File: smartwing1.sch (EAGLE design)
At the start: 27 parts, among them IC3 PIC24FJ64GB002, SW1 CT10-XXXX-A2, U1 MPL115A2, U2 MPU-6050, U3 SAM-M8Q

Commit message: Ajout_composant_axelle
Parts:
- added U$1: 992_MPL115A2, 2S_AW_lib:992_MPL115A2
- added U$2: MIKROE-2045, 2S_AW_lib:MIKROE-2045
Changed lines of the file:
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@@
 <part name="P+10" library="supply1" library_urn="urn:adsk.eagle:library:371" deviceset="VCC" device=""/>
 <part name="X_14" library="ngspice-simulation" library_urn="urn:adsk.eagle:library:527439" deviceset="GND" device=""/>
+<part name="U$1" library="2S_AW_lib" deviceset="992_MPL115A2" device=""/>
+<part name="U$2" library="2S_AW_lib" deviceset="MIKROE-2045" device=""/>
 </parts>
 <sheets>
@@
 </instance>
 <instance part="X_14" gate="G$1" x="708.66" y="15.24" smashed="yes" rot="R270"/>
+<instance part="U$1" gate="G$1" x="825.5" y="-116.84" smashed="yes">
+<attribute name="NAME" x="820.42" y="-111.76" size="1.778" layer="95"/>
+<attribute name="VALUE" x="820.42" y="-116.84" size="1.778" layer="96"/>
+</instance>
+<instance part="U$2" gate="G$1" x="894.08" y="-129.54" smashed="yes">
+<attribute name="NAME" x="889" y="-121.92" size="1.778" layer="95"/>
+<attribute name="VALUE" x="889" y="-127" size="1.778" layer="96"/>
+</instance>
 </instances>
 <busses>

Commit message: Branchements_comp_ax
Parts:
- added C12, C5: 0.1uF, rcl:C-EU075-032X103
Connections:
- removed net N$13: IC3.AN4/C1INB/DPLN/SDA2/RP2/PMD2/CN6/RB2
- removed net N$16: IC3.AN5/C1INA/DMLN/RTCC/SCL2/RP3/PMWR/CN7/RB3
- removed net N$24: IC3.TCK/USBOEN/SCL1/RP8/PMD4/CN22/RB8
- removed net N$25: IC3.TDO/SDA1/RP9/PMD3/RCV/CN21/RB9
- new net GPS_RX: U$2.RX
- new net GPS_TX: U$2.TX
- new net MPL_SCL: IC3.TCK/USBOEN/SCL1/RP8/PMD4/CN22/RB8, U$1.SCL
- new net MPL_SDA: IC3.TDO/SDA1/RP9/PMD3/RCV/CN21/RB9, U$1.SDA
- net 0: now also U$2.GND2
- net GND: now also C12.2, C5.2, U$1.GND, U$2.GND
- net VCC: now also C12.1, C5.1, U$1.VDD, U$2.3.3V
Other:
- note added: "14/06/2020"
- note added: "2S8"
- moved on the sheet: U$1, U$2

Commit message: on komance ah avouare un vurai truk
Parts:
- removed U1: MPL115A2, untitled:MPL115A2
- removed U3: SAM-M8Q, SAM_M8Q:SAM-M8Q
- added C13: 0.1uF, rcl:C-EU075-032X103
- added R4, R5, R6, R7: 4.7k, rcl:R-EU_0207/7
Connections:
- new net MPU_SCL: IC3.TCK/USBOEN/SCL1/RP8/PMD4/CN22/RB8, R6.2, U2.SCL
- new net MPU_SDA: IC3.TDO/SDA1/RP9/PMD3/RCV/CN21/RB9, R7.1, U2.SDA
- new net N$1: U$1.RST
- new net N$10: U2.NC_4
- new net N$11: U2.NC_5
- new net N$14: U2.VLOGIC
- new net N$15: U2.AD0
- new net N$16: U2.REGOUT
- new net N$19: U2.FSYNC
- new net N$20: U2.INT
- new net N$21: C13.1, U2.VDD
- new net N$24: U2.NC_6
- new net N$25: U2.NC_7
- new net N$27: U2.NC_8
- new net N$29: U2.NC
- new net N$31: U2.RESV_2
- new net N$32: U2.CPOUT
- new net N$33: U2.RESV_3
- new net N$34: U2.RESV
- new net N$37: U2.25
- new net N$9: U2.NC_3
- net GND: now also U2.GND
- net GPS_RX: now also IC3.PGEC3/AN1/C3IND/VREF-/ASCL1(2)/RP6/RA1
- net GPS_TX: now also IC3.PGED3/AN0/C3INC/VREF+/ASDA1(2)/RP5/RA0
- net MPL_SCL: now also R5.2, U2.AUX_CL; no longer IC3.TCK/USBOEN/SCL1/RP8/PMD4/CN22/RB8
- net MPL_SDA: now also R4.2, U2.AUX_DA; no longer IC3.TDO/SDA1/RP9/PMD3/RCV/CN21/RB9
- net N$3: now also U2.CLKIN; no longer IC3.PGED3/AN0/C3INC/VREF+/ASDA1(2)/RP5/RA0
- net N$4: now also U2.NC_2; no longer IC3.PGEC3/AN1/C3IND/VREF-/ASCL1(2)/RP6/RA1
- net VCC: now also C13.2, R4.1, R5.1, R6.1, R7.2

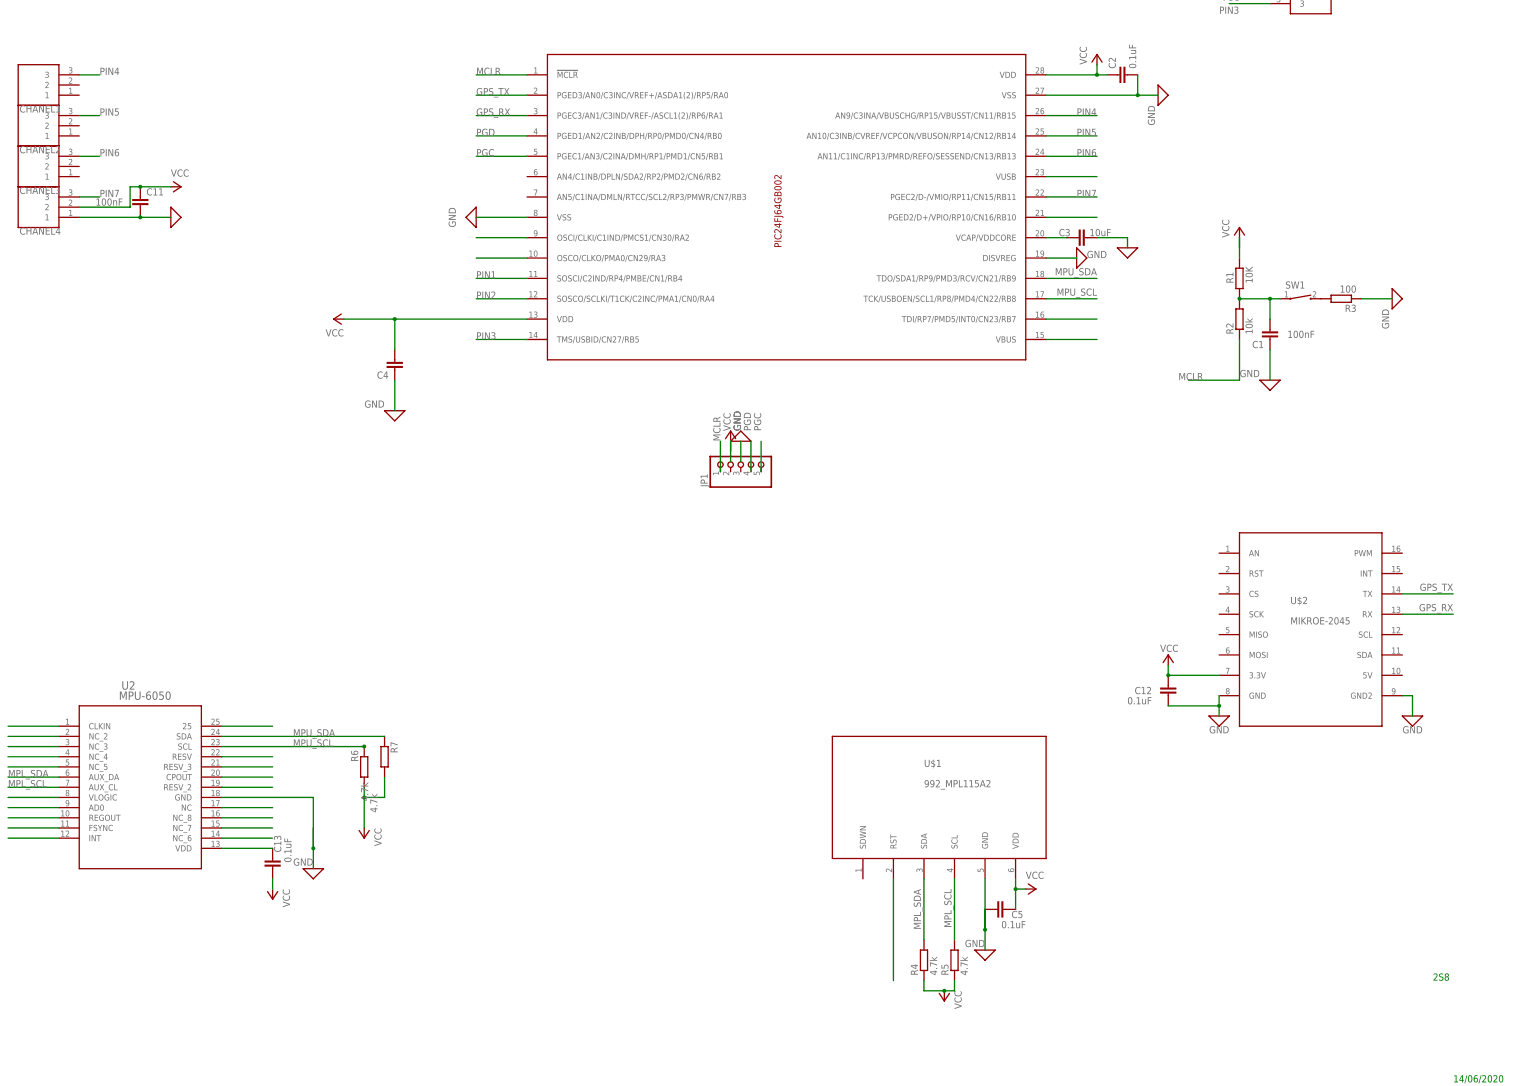
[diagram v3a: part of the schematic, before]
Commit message: Add SEN0142/UART
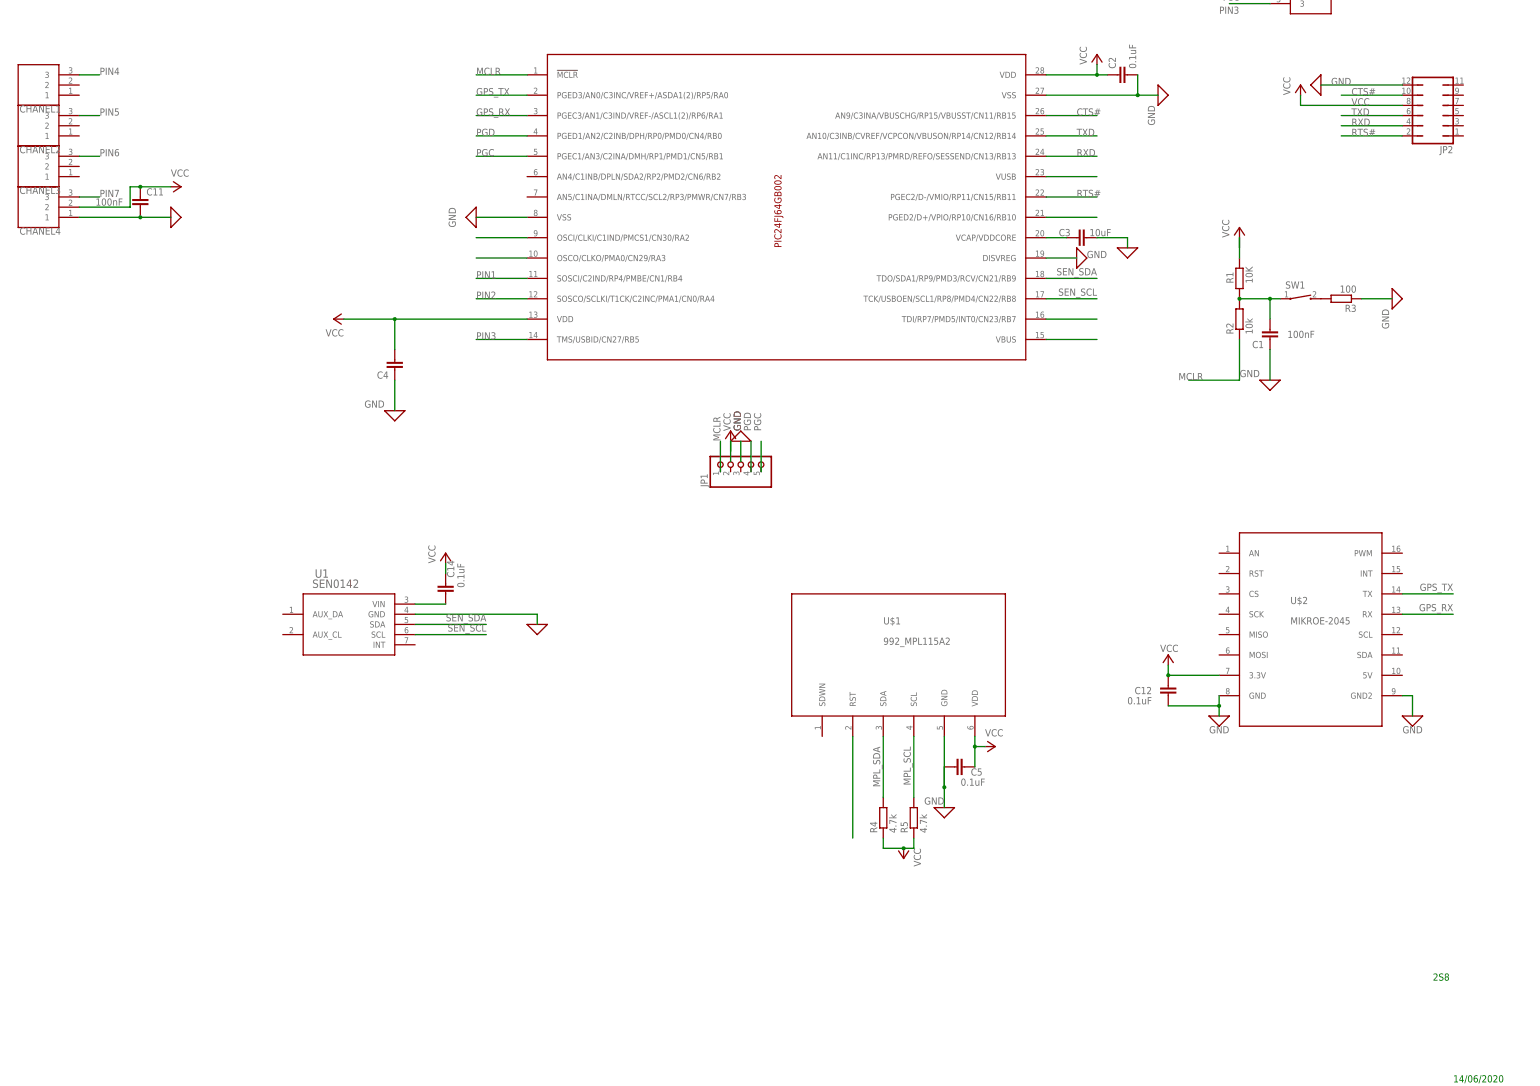
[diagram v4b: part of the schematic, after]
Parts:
- removed C13: 0.1uF, rcl:C-EU075-032X103
- removed R6, R7: 4.7k, rcl:R-EU_0207/7
- removed U2: MPU-6050, MPU6050:MPU-6050
- added C14: 0.1uF, rcl:C-EU075-032X103
- added JP2: (no value), jumper:JP6Q
- added U1: SEN0142, MPU6050:SEN0142
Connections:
- removed net MPU_SCL: IC3.TCK/USBOEN/SCL1/RP8/PMD4/CN22/RB8, R6.2, U2.SCL
- removed net MPU_SDA: IC3.TDO/SDA1/RP9/PMD3/RCV/CN21/RB9, R7.1, U2.SDA
- removed net N$10: U2.NC_4
- removed net N$11: U2.NC_5
- removed net N$14: U2.VLOGIC
- removed net N$15: U2.AD0
- removed net N$16: U2.REGOUT
- removed net N$19: U2.FSYNC
- removed net N$20: U2.INT
- removed net N$21: C13.1, U2.VDD
- removed net N$24: U2.NC_6
- removed net N$25: U2.NC_7
- removed net N$27: U2.NC_8
- removed net N$29: U2.NC
- removed net N$3: U2.CLKIN
- removed net N$31: U2.RESV_2
- removed net N$32: U2.CPOUT
- removed net N$33: U2.RESV_3
- removed net N$34: U2.RESV
- removed net N$37: U2.25
- removed net N$4: U2.NC_2
- removed net N$9: U2.NC_3
- new net CTS#: IC3.AN9/C3INA/VBUSCHG/RP15/VBUSST/CN11/RB15, JP2.10
- new net N$12: C14.2, U1.VIN
- new net RTS#: IC3.PGEC2/D-/VMIO/RP11/CN15/RB11, JP2.2
- new net RXD: IC3.AN11/C1INC/RP13/PMRD/REFO/SESSEND/CN13/RB13, JP2.4
- new net SEN_SCL: IC3.TCK/USBOEN/SCL1/RP8/PMD4/CN22/RB8, U1.SCL
- new net SEN_SDA: IC3.TDO/SDA1/RP9/PMD3/RCV/CN21/RB9, U1.SDA
- new net TXD: IC3.AN10/C3INB/CVREF/VCPCON/VBUSON/RP14/CN12/RB14, JP2.6
- net 0: now also U1.GND
- net GND: now also JP2.12; no longer U2.GND
- net MPL_SCL: no longer U2.AUX_CL
- net MPL_SDA: no longer U2.AUX_DA
- net PIN4: no longer IC3.AN9/C3INA/VBUSCHG/RP15/VBUSST/CN11/RB15
- net PIN5: no longer IC3.AN10/C3INB/CVREF/VCPCON/VBUSON/RP14/CN12/RB14
- net PIN6: no longer IC3.AN11/C1INC/RP13/PMRD/REFO/SESSEND/CN13/RB13
- net PIN7: no longer IC3.PGEC2/D-/VMIO/RP11/CN15/RB11
- net VCC: now also C14.1, JP2.8; no longer C13.2, R6.1, R7.2
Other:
- moved on the sheet: C5, R4, R5, U$1

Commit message: all pin
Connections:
- net N$23 renamed PIN8
- removed net N$17: IC3.OSCI/CLKI/C1IND/PMCS1/CN30/RA2
- removed net N$18: IC3.OSCO/CLKO/PMA0/CN29/RA3
- net CTS#: no longer IC3.AN9/C3INA/VBUSCHG/RP15/VBUSST/CN11/RB15
- net PIN4: now also IC3.OSCI/CLKI/C1IND/PMCS1/CN30/RA2
- net PIN5: now also IC3.OSCO/CLKO/PMA0/CN29/RA3
- net PIN6: now also IC3.AN9/C3INA/VBUSCHG/RP15/VBUSST/CN11/RB15
- net PIN7: now also IC3.PGEC2/D-/VMIO/RP11/CN15/RB11
- net RTS#: no longer IC3.PGEC2/D-/VMIO/RP11/CN15/RB11
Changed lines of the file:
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@@
 <?xml version="1.0" encoding="utf-8"?>
 <!DOCTYPE eagle SYSTEM "eagle.dtd">
-<eagle version="9.6.2">
+<eagle version="9.6.1">
 <drawing>
 <settings>
@@
 <label x="614.68" y="50.8" size="1.778" layer="95"/>
 </segment>
+<segment>
+<pinref part="IC3" gate="G$1" pin="OSCI/CLKI/C1IND/PMCS1/CN30/RA2"/>
+<wire x1="721.36" y1="10.16" x2="708.66" y2="10.16" width="0.1524" layer="91"/>
+<label x="706.12" y="10.16" size="1.778" layer="95"/>
+</segment>
 </net>
 <net name="VCC2" class="0">
@@
 <label x="614.68" y="40.64" size="1.778" layer="95"/>
 </segment>
+<segment>
+<pinref part="IC3" gate="G$1" pin="OSCO/CLKO/PMA0/CN29/RA3"/>
+<wire x1="721.36" y1="5.08" x2="708.66" y2="5.08" width="0.1524" layer="91"/>
+<label x="706.12" y="5.08" size="1.778" layer="95"/>
+</segment>
 </net>
 <net name="VCC3" class="0">
@@
 <label x="614.68" y="30.48" size="1.778" layer="95"/>
 </segment>
+<segment>
+<pinref part="IC3" gate="G$1" pin="AN9/C3INA/VBUSCHG/RP15/VBUSST/CN11/RB15"/>
+<wire x1="850.9" y1="40.64" x2="863.6" y2="40.64" width="0.1524" layer="91"/>
+<label x="858.52" y="40.64" size="1.778" layer="95"/>
+</segment>
 </net>
 <net name="PIN7" class="0">
@@
 <label x="614.68" y="20.32" size="1.778" layer="95"/>
 </segment>
+<segment>
+<pinref part="IC3" gate="G$1" pin="PGEC2/D-/VMIO/RP11/CN15/RB11"/>
+<wire x1="850.9" y1="20.32" x2="863.6" y2="20.32" width="0.1524" layer="91"/>
+<label x="858.52" y="20.32" size="1.778" layer="95"/>
+</segment>
 </net>
 <net name="N$2" class="0">
@@
 </segment>
 </net>
-<net name="N$17" class="0">
-<segment>
-<pinref part="IC3" gate="G$1" pin="OSCI/CLKI/C1IND/PMCS1/CN30/RA2"/>
-<wire x1="721.36" y1="10.16" x2="708.66" y2="10.16" width="0.1524" layer="91"/>
-</segment>
-</net>
-<net name="N$18" class="0">
-<segment>
-<pinref part="IC3" gate="G$1" pin="OSCO/CLKO/PMA0/CN29/RA3"/>
-<wire x1="721.36" y1="5.08" x2="708.66" y2="5.08" width="0.1524" layer="91"/>
-</segment>
-</net>
 <net name="N$22" class="0">
 <segment>
@@
 </segment>
 </net>
-<net name="N$23" class="0">
+<net name="PIN8" class="0">
 <segment>
 <pinref part="IC3" gate="G$1" pin="TDI/RP7/PMD5/INT0/CN23/RB7"/>
 <wire x1="850.9" y1="-10.16" x2="863.6" y2="-10.16" width="0.1524" layer="91"/>
+<label x="858.52" y="-10.16" size="1.778" layer="95"/>
 </segment>
 </net>
@@
 <pinref part="IC3" gate="G$1" pin="PGED2/D+/VPIO/RP10/CN16/RB10"/>
 <wire x1="850.9" y1="15.24" x2="863.6" y2="15.24" width="0.1524" layer="91"/>
+<label x="858.52" y="15.24" size="1.778" layer="95"/>
 </segment>
 </net>
@@
 <label x="927.1" y="45.72" size="1.778" layer="95" grouprefs="UART"/>
 </segment>
-<segment>
-<pinref part="IC3" gate="G$1" pin="AN9/C3INA/VBUSCHG/RP15/VBUSST/CN11/RB15"/>
-<wire x1="850.9" y1="40.64" x2="863.6" y2="40.64" width="0.1524" layer="91"/>
-<label x="858.52" y="40.64" size="1.778" layer="95"/>
-</segment>
 </net>
 <net name="TXD" class="0">
@@
 <label x="927.1" y="35.56" size="1.778" layer="95" grouprefs="UART"/>
 </segment>
-<segment>
-<pinref part="IC3" gate="G$1" pin="PGEC2/D-/VMIO/RP11/CN15/RB11"/>
-<wire x1="850.9" y1="20.32" x2="863.6" y2="20.32" width="0.1524" layer="91"/>
-<label x="858.52" y="20.32" size="1.778" layer="95"/>
-</segment>
-</net>
+</net>

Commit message: quelques correction
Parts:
- removed JP2: (no value), jumper:JP6Q
- added C13, C15, C16, C17, C18, C19, C20, C21, C22, C23, C24, C25, C26, C27, C28, C29: 100nF, rcl:C-EU075-032X103
- added IC1: (no value), v-reg:78LXX
- added R10, R11, R12, R6, R7, R8, R9: 4.7k, rcl:R-EU_0207/7
- added U2, U3, U4, U5, U6, U7, U8: SN74LVC1T45DBVT, NEWCUSTOM:SN74LVC1T45DBVT
- R2: value 10k -> 1k
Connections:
- removed net CTS#: JP2.10
- removed net PIN1: ESC1.3, IC3.SOSCI/C2IND/RP4/PMBE/CN1/RB4
- removed net PIN2: IC3.SOSCO/SCLKI/T1CK/C2INC/PMA1/CN0/RA4, SERVOMOTEUR1.3
- removed net PIN3: IC3.TMS/USBID/CN27/RB5, SERVOMOTEUR2.3
- removed net RTS#: JP2.2
- new net N$10: R9.2, U2.DIR
- new net N$11: R6.2, U8.DIR
- new net N$13: C17.1, C19.1, C21.1, C23.1, C25.1, C27.1, C29.1, U2.VCCB, U3.VCCB, U4.VCCB, U5.VCCB, U6.VCCB, U7.VCCB, U8.VCCB
- new net N$14: R10.2, U5.DIR
- new net N$15: R11.2, U6.DIR
- new net N$16: R12.2, U7.DIR
- new net N$17: U$1.SDWN
- new net N$3: C16.1, C18.1, C20.1, C22.1, C24.1, C26.1, C28.1, U2.VCCA, U3.VCCA, U4.VCCA, U5.VCCA, U6.VCCA, U7.VCCA, U8.VCCA
- new net N$4: R7.2, U3.DIR
- new net N$9: R8.2, U4.DIR
- new net PWM_CHANEL1_3V: IC3.OSCI/CLKI/C1IND/PMCS1/CN30/RA2, U2.A
- new net PWM_CHANEL1_5V: U2.B
- new net PWM_CHANEL2_3V: IC3.OSCO/CLKO/PMA0/CN29/RA3, U5.A
- new net PWM_CHANEL2_5V: U5.B
- new net PWM_CHANEL3_3V: IC3.AN9/C3INA/VBUSCHG/RP15/VBUSST/CN11/RB15, U6.A
- new net PWM_CHANEL3_5V: U6.B
- new net PWM_CHANEL4_3V: IC3.PGEC2/D-/VMIO/RP11/CN15/RB11, U7.A
- new net PWM_CHANEL4_5V: U7.B
- new net PWM_ESC_3V: IC3.SOSCI/C2IND/RP4/PMBE/CN1/RB4, U8.B
- new net PWM_ESC_5V: ESC1.3, U8.A
- new net PWM_SERVO1_3V: IC3.SOSCO/SCLKI/T1CK/C2INC/PMA1/CN0/RA4, U4.B
- new net PWM_SERVO1_5V: SERVOMOTEUR1.3, U4.A
- new net PWM_SERVO2_3V: IC3.TMS/USBID/CN27/RB5, U3.B
- new net PWM_SERVO2_5V: SERVOMOTEUR2.3, U3.A
- new net VCC1: C10.2, C11.1, C8.1, C9.2, CHANEL4.2, ESC1.2, SERVOMOTEUR1.2, SERVOMOTEUR2.2
- net 0: now also C14.2, C17.2, C19.2, C21.2, C23.2, C25.2, C27.2, C29.2, R10.1, R11.1, R12.1, R6.1, R7.1, R8.1, R9.1
- net GND: no longer JP2.12
- net N$12: now also C14.1; no longer C14.2
- net N$6: now also C13.2, C15.1, C16.2, C18.2, C20.2, C22.2, C24.2, C26.2, C28.2, IC1.GND, U2.GND, U3.GND, U4.GND, U5.GND, U6.GND, U7.GND, U8.GND
- net N$8: now also C15.2, IC1.OUT
- net PIN4: no longer IC3.OSCI/CLKI/C1IND/PMCS1/CN30/RA2
- net PIN5: no longer IC3.OSCO/CLKO/PMA0/CN29/RA3
- net PIN6: no longer IC3.AN9/C3INA/VBUSCHG/RP15/VBUSST/CN11/RB15
- net PIN7: no longer IC3.PGEC2/D-/VMIO/RP11/CN15/RB11
- net RXD: no longer JP2.4
- net TXD: no longer JP2.6
- net VBAT: now also C13.1, IC1.IN
- net VCC: no longer C10.2, C11.1, C14.1, C8.1, C9.2, CHANEL4.2, ESC1.2, JP2.8, SERVOMOTEUR1.2, SERVOMOTEUR2.2
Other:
- note added: "VCC1 = 5V"
- moved on the sheet: C11, C14, C6, C7, C8, CHANEL1, CHANEL2, CHANEL3, CHANEL4, ESC1, IC2

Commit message: sq
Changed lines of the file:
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@@
 <?xml version="1.0" encoding="utf-8"?>
 <!DOCTYPE eagle SYSTEM "eagle.dtd">
-<eagle version="9.6.1">
+<eagle version="9.6.2">
 <drawing>
 <settings>
@@
 <part name="C1" library="rcl" library_urn="urn:adsk.eagle:library:334" deviceset="C-EU" device="075-032X103" package3d_urn="urn:adsk.eagle:package:23646/1" value="100nF"/>
 <part name="P+2" library="supply1" library_urn="urn:adsk.eagle:library:371" deviceset="VCC" device=""/>
-<part name="P+3" library="supply1" library_urn="urn:adsk.eagle:library:371" deviceset="VCC" device=""/>
 <part name="P+4" library="supply1" library_urn="urn:adsk.eagle:library:371" deviceset="VCC" device=""/>
 <part name="P+5" library="supply1" library_urn="urn:adsk.eagle:library:371" deviceset="VCC" device=""/>
@@
 </instance>
 <instance part="P+2" gate="VCC" x="896.62" y="71.12" smashed="yes" rot="R90" grouprefs="SERVO"/>
-<instance part="P+3" gate="VCC" x="792.48" y="167.64" smashed="yes" rot="R180" grouprefs="BRUSHLESS"/>
 <instance part="P+4" gate="VCC" x="568.96" y="43.18" smashed="yes" rot="R270" grouprefs="RX"/>
 <instance part="P+5" gate="VCC" x="899.16" y="12.7" smashed="yes" grouprefs="REST">
@@
 </segment>
 <segment>
-<pinref part="P+3" gate="VCC" pin="VCC"/>
-<wire x1="792.48" y1="170.18" x2="792.48" y2="175.26" width="0.1524" layer="91" grouprefs="BRUSHLESS"/>
 <pinref part="ESC1" gate="G$1" pin="2"/>
 <pinref part="C8" gate="G$1" pin="1"/>
 <wire x1="792.48" y1="175.26" x2="792.48" y2="187.96" width="0.1524" layer="91" grouprefs="BRUSHLESS"/>
-<junction x="792.48" y="175.26"/>
-<label x="792.48" y="172.72" size="1.778" layer="95"/>
-</segment>
-<segment>
+</segment>
+<segment>
